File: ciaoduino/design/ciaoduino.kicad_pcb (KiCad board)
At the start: 2 copper layers, 76.4 x 76.4 mm, 17 parts, among them P1 ICSP, P2 CONN_01X02, P3 USB_OTG, P4 CONN_01X06, P5 CONN_01X06, P6 CONN_01X04, P7 CONN_01X14, SW1 SW_PUSH, SW2 SW_PUSH, U2 ATmega32U4-AU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

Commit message: Update board with UCAP pad connected.
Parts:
- added C3: C, Capacitors_SMD:C_0603_HandSoldering, F.Cu at (137.9, 77.2)
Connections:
- U2 pad 5: (no net) -> GND
- U2 pad 6: (no net) -> Net-(C3-Pad2)
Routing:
- net Net-(C3-Pad2): track 0.00 -> 8.06 mm
- net GND: track 12.3 -> 15.1 mm
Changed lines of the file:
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@@
 (kicad_pcb (version 4) (host pcbnew 4.0.2+dfsg1-stable)
   (general
-    (links 75)
+    (links 78)
     (no_connects 0)
     (area 112.579273 43.237273 189.172727 119.830727)
     (thickness 1.6)
     (drawings 4)
-    (tracks 250)
+    (tracks 257)
     (zones 0)
-    (modules 17)
-    (nets 34)
+    (modules 18)
+    (nets 35)
   )
   (page A4)
@@
   (net 32 ADC12)
   (net 33 ADC13)
+  (net 34 "Net-(C3-Pad2)")
   (net_class Default "This is the default net class."
     (clearance 0.2)
@@
     (add_net "Net-(C1-Pad1)")
     (add_net "Net-(C2-Pad1)")
+    (add_net "Net-(C3-Pad2)")
     (add_net "Net-(P3-Pad2)")
     (add_net "Net-(P3-Pad3)")
@@
     (pad 4 smd rect (at -5.7 -1.6) (size 1.5 0.55) (layers F.Cu F.Paste F.Mask)
       (net 7 "Net-(R3-Pad1)"))
-    (pad 5 smd rect (at -5.7 -0.8) (size 1.5 0.55) (layers F.Cu F.Paste F.Mask))
-    (pad 6 smd rect (at -5.7 0) (size 1.5 0.55) (layers F.Cu F.Paste F.Mask))
+    (pad 5 smd rect (at -5.7 -0.8) (size 1.5 0.55) (layers F.Cu F.Paste F.Mask)
+      (net 2 GND))
+    (pad 6 smd rect (at -5.7 0) (size 1.5 0.55) (layers F.Cu F.Paste F.Mask)
+      (net 34 "Net-(C3-Pad2)"))
     (pad 7 smd rect (at -5.7 0.8) (size 1.5 0.55) (layers F.Cu F.Paste F.Mask)
       (net 5 VCC))
@@
     )
   )
+  (module Capacitors_SMD:C_0603_HandSoldering (layer F.Cu)
+    (at 137.922 77.216 90)
+    (descr "Capacitor SMD 0603, hand soldering")
+    (tags "capacitor 0603")
+    (attr smd)
+    (fp_text reference C3 (at 0 -1.9 90) (layer F.SilkS)
+      (effects (font (size 1 1) (thickness 0.15)))
+    )
+    (fp_text value C (at 0 1.9 90) (layer F.Fab)
+      (effects (font (size 1 1) (thickness 0.15)))
+    )
+    (fp_line (start -1.85 -0.75) (end 1.85 -0.75) (layer F.CrtYd) (width 0.05))
+    (fp_line (start -1.85 0.75) (end 1.85 0.75) (layer F.CrtYd) (width 0.05))
+    (fp_line (start -1.85 -0.75) (end -1.85 0.75) (layer F.CrtYd) (width 0.05))
+    (fp_line (start 1.85 -0.75) (end 1.85 0.75) (layer F.CrtYd) (width 0.05))
+    (fp_line (start -0.35 -0.6) (end 0.35 -0.6) (layer F.SilkS) (width 0.15))
+    (fp_line (start 0.35 0.6) (end -0.35 0.6) (layer F.SilkS) (width 0.15))
+    (pad 1 smd rect (at -0.95 0 90) (size 1.2 0.75) (layers F.Cu F.Paste F.Mask)
+      (net 2 GND))
+    (pad 2 smd rect (at 0.95 0 90) (size 1.2 0.75) (layers F.Cu F.Paste F.Mask)
+      (net 34 "Net-(C3-Pad2)"))
+    (model Capacitors_SMD.3dshapes/C_0603_HandSoldering.wrl
+      (at (xyz 0 0 0))
+      (scale (xyz 1 1 1))
+      (rotate (xyz 0 0 0))
+    )
+  )
   (dimension 51.054632 (width 0.3) (layer Dwgs.User)
     (gr_text "51,055 mm" (at 152.572939 123.660896 0.2850512776) (layer Dwgs.User)
@@
   (segment (start 152.23 83.904) (end 151.13 82.804) (width 0.1524) (layer F.Cu) (net 1))
   (segment (start 156.06 86.83) (end 156.21 86.68) (width 0.1524) (layer F.Cu) (net 1))
+  (segment (start 145.43 74.13) (end 143.04 74.13) (width 0.1524) (layer F.Cu) (net 2) (status 400000))
+  (segment (start 143.04 74.13) (end 142.748 74.422) (width 0.1524) (layer F.Cu) (net 2))
   (segment (start 154.33 69.23) (end 154.33 67.158) (width 0.1524) (layer F.Cu) (net 2))
   (segment (start 154.33 67.158) (end 154.94 66.548) (width 0.1524) (layer F.Cu) (net 2))
@@
   (segment (start 147.93 69.23) (end 147.93 71.476) (width 0.1524) (layer F.Cu) (net 2))
   (segment (start 147.93 71.476) (end 148.336 71.882) (width 0.1524) (layer F.Cu) (net 2))
-  (segment (start 150.33 80.63) (end 150.33 82.842) (width 0.1524) (layer F.Cu) (net 3) (status 400000))
-  (segment (start 146.05 85.09) (end 146.05 86.68) (width 0.1524) (layer F.Cu) (net 3) (status 800000))
+  (segment (start 150.33 80.63) (end 150.33 82.842) (width 0.1524) (layer F.Cu) (net 3))
+  (segment (start 146.05 85.09) (end 146.05 86.68) (width 0.1524) (layer F.Cu) (net 3))
   (via (at 146.05 85.09) (size 0.6) (drill 0.4) (layers F.Cu B.Cu) (net 3))
   (segment (start 146.304 85.09) (end 146.05 85.09) (width 0.1524) (layer B.Cu) (net 3))
@@
   (segment (start 146.37 86.68) (end 148.12 88.43) (width 0.1524) (layer F.Cu) (net 3))
   (segment (start 148.12 88.43) (end 150.03 88.43) (width 0.1524) (layer F.Cu) (net 3))
-  (segment (start 145.43 78.93) (end 145.43 79.898) (width 0.1524) (layer F.Cu) (net 4) (status 400000))
-  (segment (start 136.398 90.17) (end 134.112 87.884) (width 0.1524) (layer F.Cu) (net 4) (status 800000))
+  (segment (start 145.43 78.93) (end 145.43 79.898) (width 0.1524) (layer F.Cu) (net 4))
+  (segment (start 136.398 90.17) (end 134.112 87.884) (width 0.1524) (layer F.Cu) (net 4))
   (segment (start 140.462 90.17) (end 136.398 90.17) (width 0.1524) (layer F.Cu) (net 4))
   (segment (start 141.732 88.9) (end 140.462 90.17) (width 0.1524) (layer F.Cu) (net 4))
@@
   (segment (start 128.66116 79.38008) (end 128.66116 70.47992) (width 0.1524) (layer F.Cu) (net 11))
   (segment (start 128.66116 70.47992) (end 134.16026 70.47992) (width 0.1524) (layer F.Cu) (net 11))
-  (segment (start 147.13 80.63) (end 147.13 81.724) (width 0.1524) (layer F.Cu) (net 12) (status 400000))
+  (segment (start 147.13 80.63) (end 147.13 81.724) (width 0.1524) (layer F.Cu) (net 12))
   (segment (start 176.352523 89.992523) (end 176.352523 93.98) (width 0.1524) (layer F.Cu) (net 12))
   (segment (start 170.688 84.328) (end 176.352523 89.992523) (width 0.1524) (layer F.Cu) (net 12))
@@
   (via (at 154.686 72.644) (size 0.6) (drill 0.4) (layers F.Cu B.Cu) (net 33))
   (segment (start 158.496 68.834) (end 154.686 72.644) (width 0.1524) (layer B.Cu) (net 33))
+  (segment (start 145.43 74.93) (end 144.018 74.93) (width 0.1524) (layer F.Cu) (net 34) (status 400000))
+  (segment (start 141.158 76.266) (end 137.922 76.266) (width 0.1524) (layer F.Cu) (net 34) (status 800000))
+  (segment (start 141.732 75.692) (end 141.158 76.266) (width 0.1524) (layer F.Cu) (net 34))
+  (segment (start 143.256 75.692) (end 141.732 75.692) (width 0.1524) (layer F.Cu) (net 34))
+  (segment (start 144.018 74.93) (end 143.256 75.692) (width 0.1524) (layer F.Cu) (net 34))
   (zone (net 2) (net_name GND) (layer F.Cu) (hatch edge 0.508)
     (connect_pads (clearance 0.4))

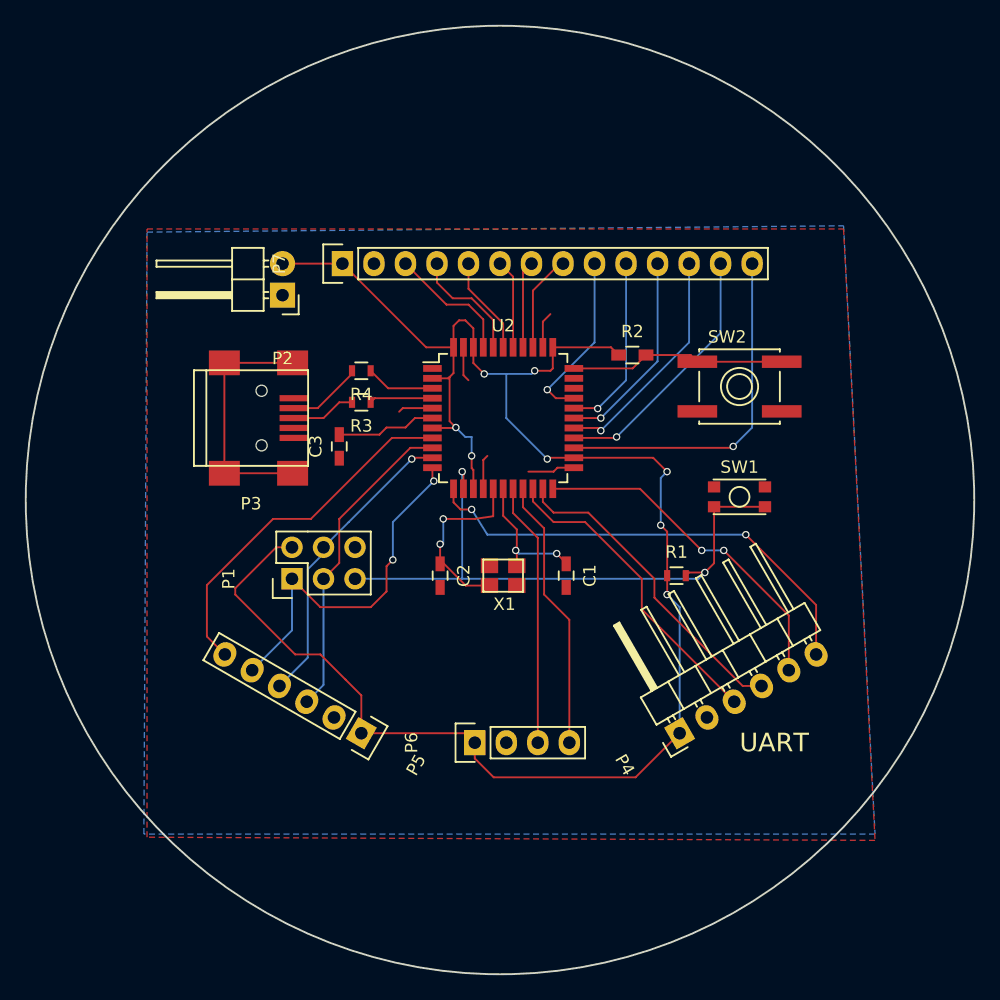
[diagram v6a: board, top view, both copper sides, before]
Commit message: Add mounting hole and reworked edges.
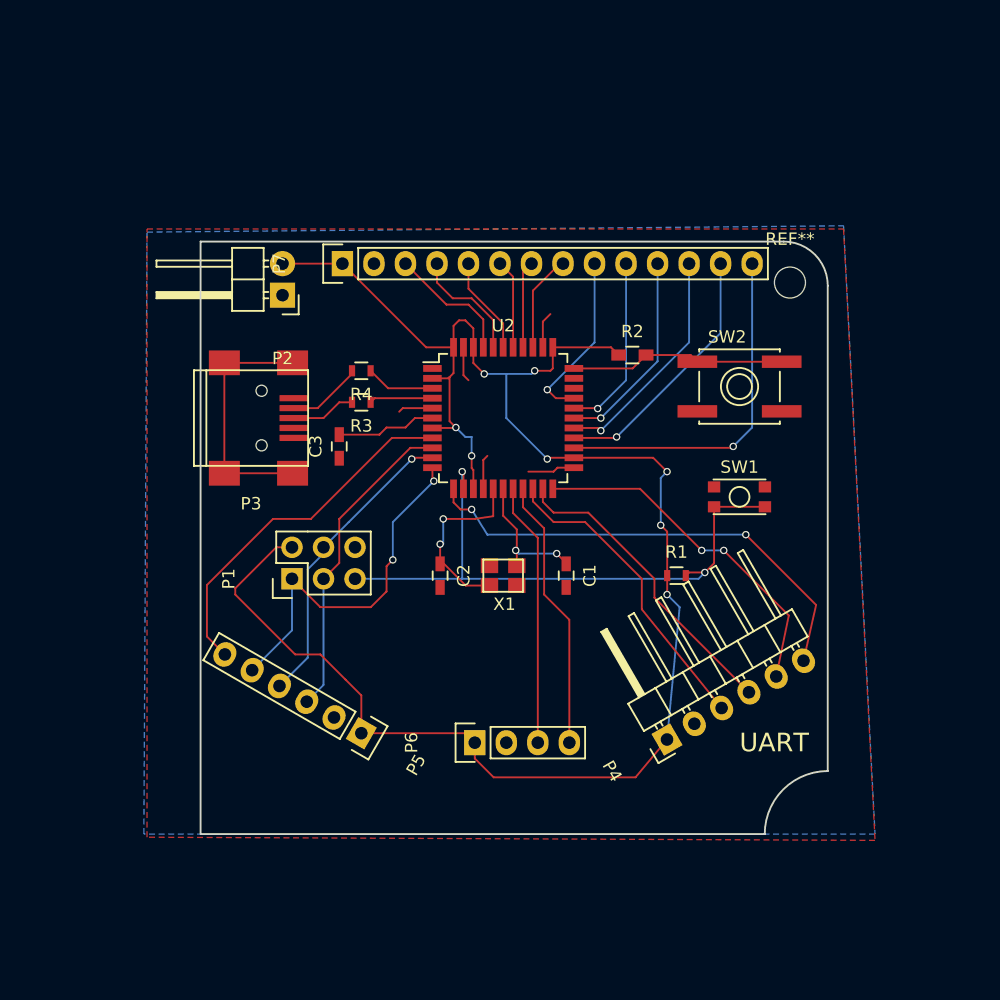
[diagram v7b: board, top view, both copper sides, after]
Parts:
- added REF**: MountingHole_2.5mm, Mounting_Holes:MountingHole_2.5mm, F.Cu at (174.2, 64.0)
- moved P4 1.14 mm to (164.3, 100.8)
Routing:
- net usart_tx: track 25.7 -> 24.9 mm
- net usart_rts: track 38.0 -> 38.6 mm
- net usart_cts: track 27.7 -> 28.3 mm
- net VCC: track 146.0 -> 145.5 mm
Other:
- board size 76.4 x 76.4 mm -> 50.5 x 47.8 mm
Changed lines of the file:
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@@
   (general
     (links 78)
-    (no_connects 0)
-    (area 112.579273 43.237273 189.172727 119.830727)
+    (no_connects 1)
+    (area 126.670999 60.630999 177.367001 108.533001)
     (thickness 1.6)
-    (drawings 4)
+    (drawings 9)
     (tracks 257)
     (zones 0)
-    (modules 18)
+    (modules 19)
     (nets 35)
   )
@@
     (39 F.Mask user)
     (40 Dwgs.User user)
-    (41 Cmts.User user)
-    (42 Eco1.User user)
-    (43 Eco2.User user)
+    (41 Cmts.User user hide)
+    (42 Eco1.User user hide)
+    (43 Eco2.User user hide)
     (44 Edge.Cuts user)
     (45 Margin user)
-    (46 B.CrtYd user)
-    (47 F.CrtYd user)
-    (48 B.Fab user)
-    (49 F.Fab user)
+    (46 B.CrtYd user hide)
+    (47 F.CrtYd user hide)
+    (48 B.Fab user hide)
+    (49 F.Fab user hide)
   )
   (setup
@@
   )
   (module Pin_Headers:Pin_Header_Angled_1x06 (layer F.Cu)
-    (at 165.354 100.33 120)
+    (at 164.338 100.838 120)
     (descr "Through hole pin header")
     (tags "pin header")
@@
     )
   )
+  (module Mounting_Holes:MountingHole_2.5mm (layer F.Cu)
+    (at 174.244 64.008)
+    (descr "Mounting Hole 2.5mm, no annular")
+    (tags "mounting hole 2.5mm no annular")
+    (fp_text reference REF** (at 0 -3.5) (layer F.SilkS)
+      (effects (font (size 1 1) (thickness 0.15)))
+    )
+    (fp_text value MountingHole_2.5mm (at 0 3.5) (layer F.Fab)
+      (effects (font (size 1 1) (thickness 0.15)))
+    )
+    (fp_circle (center 0 0) (end 2.5 0) (layer Cmts.User) (width 0.15))
+    (fp_circle (center 0 0) (end 2.75 0) (layer F.CrtYd) (width 0.05))
+    (pad 1 np_thru_hole circle (at 0 0) (size 2.5 2.5) (drill 2.5) (layers *.Cu *.Mask F.SilkS))
+  )
+  (gr_line (start 126.746 108.458) (end 172.212 108.458) (angle 90) (layer Edge.Cuts) (width 0.15))
+  (gr_line (start 173.736 60.706) (end 126.746 60.706) (angle 90) (layer Edge.Cuts) (width 0.15))
+  (gr_line (start 126.746 108.458) (end 126.746 60.706) (angle 90) (layer Edge.Cuts) (width 0.15))
+  (gr_arc (start 177.292 108.458) (end 172.212 108.458) (angle 90) (layer Edge.Cuts) (width 0.15))
+  (gr_line (start 177.292 64.262) (end 177.292 103.378) (angle 90) (layer Edge.Cuts) (width 0.15))
+  (gr_arc (start 173.736 64.262) (end 173.736 60.706) (angle 90) (layer Edge.Cuts) (width 0.15))
   (dimension 51.054632 (width 0.3) (layer Dwgs.User)
     (gr_text "51,055 mm" (at 152.572939 123.660896 0.2850512776) (layer Dwgs.User)
@@
     (effects (font (size 1.5 1.5) (thickness 0.3)))
   )
-  (gr_circle (center 150.876 81.534) (end 135.636 46.482) (layer Edge.Cuts) (width 0.15))
   (segment (start 152.23 85.598) (end 152.146 85.598) (width 0.1524) (layer F.Cu) (net 1))
   (segment (start 155.448 85.852) (end 156.21 86.614) (width 0.1524) (layer F.Cu) (net 1))
@@
   (segment (start 152.23 83.904) (end 151.13 82.804) (width 0.1524) (layer F.Cu) (net 1))
   (segment (start 156.06 86.83) (end 156.21 86.68) (width 0.1524) (layer F.Cu) (net 1))
-  (segment (start 145.43 74.13) (end 143.04 74.13) (width 0.1524) (layer F.Cu) (net 2) (status 400000))
+  (segment (start 149.53 80.63) (end 149.53 78.308) (width 0.1524) (layer F.Cu) (net 2))
+  (segment (start 145.43 74.13) (end 143.04 74.13) (width 0.1524) (layer F.Cu) (net 2))
   (segment (start 143.04 74.13) (end 142.748 74.422) (width 0.1524) (layer F.Cu) (net 2))
   (segment (start 154.33 69.23) (end 154.33 67.158) (width 0.1524) (layer F.Cu) (net 2))
   (segment (start 154.33 67.158) (end 154.94 66.548) (width 0.1524) (layer F.Cu) (net 2))
-  (segment (start 149.53 80.63) (end 149.53 78.308) (width 0.1524) (layer F.Cu) (net 2))
   (segment (start 149.53 78.308) (end 149.86 77.978) (width 0.1524) (layer F.Cu) (net 2))
   (segment (start 156.83 78.93) (end 155.512 78.93) (width 0.1524) (layer F.Cu) (net 2))
@@
   (segment (start 134.112 92.039182) (end 130.901182 95.25) (width 0.1524) (layer B.Cu) (net 4))
   (segment (start 164.35 87.63) (end 164.35 89.142) (width 0.1524) (layer F.Cu) (net 5))
-  (segment (start 165.354 90.17) (end 165.354 100.33) (width 0.1524) (layer B.Cu) (net 5))
+  (segment (start 165.354 90.17) (end 164.338 100.838) (width 0.1524) (layer B.Cu) (net 5) (status 20))
   (segment (start 164.338 89.154) (end 165.354 90.17) (width 0.1524) (layer B.Cu) (net 5))
   (via (at 164.338 89.154) (size 0.6) (drill 0.4) (layers F.Cu B.Cu) (net 5))
@@
   (segment (start 148.844 102.362) (end 150.368 103.886) (width 0.1524) (layer F.Cu) (net 5))
   (segment (start 150.368 103.886) (end 161.798 103.886) (width 0.1524) (layer F.Cu) (net 5))
-  (segment (start 161.798 103.886) (end 165.354 100.33) (width 0.1524) (layer F.Cu) (net 5))
+  (segment (start 161.798 103.886) (end 164.338 100.838) (width 0.1524) (layer F.Cu) (net 5) (status 20))
   (segment (start 139.7 100.33) (end 148.082 100.33) (width 0.1524) (layer F.Cu) (net 5))
   (segment (start 148.082 100.33) (end 148.844 101.092) (width 0.1524) (layer F.Cu) (net 5))
@@
   (segment (start 128.66116 70.47992) (end 134.16026 70.47992) (width 0.1524) (layer F.Cu) (net 11))
   (segment (start 147.13 80.63) (end 147.13 81.724) (width 0.1524) (layer F.Cu) (net 12))
-  (segment (start 176.352523 89.992523) (end 176.352523 93.98) (width 0.1524) (layer F.Cu) (net 12))
+  (segment (start 176.352523 89.992523) (end 175.336523 94.488) (width 0.1524) (layer F.Cu) (net 12) (status 20))
   (segment (start 170.688 84.328) (end 176.352523 89.992523) (width 0.1524) (layer F.Cu) (net 12))
   (via (at 170.688 84.328) (size 0.6) (drill 0.4) (layers F.Cu B.Cu) (net 12))
@@
   (segment (start 147.13 81.724) (end 147.702 82.296) (width 0.1524) (layer F.Cu) (net 12))
   (segment (start 153.53 80.63) (end 153.53 81.648) (width 0.1524) (layer F.Cu) (net 13))
-  (segment (start 162.306 90.342591) (end 169.753409 97.79) (width 0.1524) (layer F.Cu) (net 13))
+  (segment (start 162.306 90.342591) (end 168.737409 98.298) (width 0.1524) (layer F.Cu) (net 13) (status 20))
   (segment (start 162.306 87.884) (end 162.306 90.342591) (width 0.1524) (layer F.Cu) (net 13))
   (segment (start 157.734 83.312) (end 162.306 87.884) (width 0.1524) (layer F.Cu) (net 13))
@@
   (segment (start 153.53 81.648) (end 155.194 83.312) (width 0.1524) (layer F.Cu) (net 13))
   (segment (start 154.33 80.63) (end 154.33 81.686) (width 0.1524) (layer F.Cu) (net 14))
-  (segment (start 170.434 96.52) (end 171.953114 96.52) (width 0.1524) (layer F.Cu) (net 14))
+  (segment (start 170.434 96.52) (end 170.937114 97.028) (width 0.1524) (layer F.Cu) (net 14) (status 20))
   (segment (start 163.322 89.408) (end 170.434 96.52) (width 0.1524) (layer F.Cu) (net 14))
   (segment (start 163.322 87.884) (end 163.322 89.408) (width 0.1524) (layer F.Cu) (net 14))
@@
   (segment (start 154.33 81.686) (end 155.194 82.55) (width 0.1524) (layer F.Cu) (net 14))
   (segment (start 155.13 80.63) (end 162.164 80.63) (width 0.1524) (layer F.Cu) (net 15))
-  (segment (start 174.152818 90.840818) (end 174.152818 95.25) (width 0.1524) (layer F.Cu) (net 15))
+  (segment (start 174.152818 90.840818) (end 173.136818 95.758) (width 0.1524) (layer F.Cu) (net 15) (status 20))
   (segment (start 168.91 85.598) (end 174.152818 90.840818) (width 0.1524) (layer F.Cu) (net 15))
   (via (at 168.91 85.598) (size 0.6) (drill 0.4) (layers F.Cu B.Cu) (net 15))
@@
   (via (at 154.686 72.644) (size 0.6) (drill 0.4) (layers F.Cu B.Cu) (net 33))
   (segment (start 158.496 68.834) (end 154.686 72.644) (width 0.1524) (layer B.Cu) (net 33))
-  (segment (start 145.43 74.93) (end 144.018 74.93) (width 0.1524) (layer F.Cu) (net 34) (status 400000))
-  (segment (start 141.158 76.266) (end 137.922 76.266) (width 0.1524) (layer F.Cu) (net 34) (status 800000))
+  (segment (start 145.43 74.93) (end 144.018 74.93) (width 0.1524) (layer F.Cu) (net 34))
+  (segment (start 141.158 76.266) (end 137.922 76.266) (width 0.1524) (layer F.Cu) (net 34))
   (segment (start 141.732 75.692) (end 141.158 76.266) (width 0.1524) (layer F.Cu) (net 34))
   (segment (start 143.256 75.692) (end 141.732 75.692) (width 0.1524) (layer F.Cu) (net 34))
